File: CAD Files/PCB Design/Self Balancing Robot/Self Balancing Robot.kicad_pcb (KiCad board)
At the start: 2 copper layers, 14 parts, among them J1 Screw_Terminal_01x02, M1 Stepper_Motor_bipolar, M2 Stepper_Motor_bipolar, U1 DEVKIT_V1_ESP32-WROOM-32, U2 TSR_1-2450

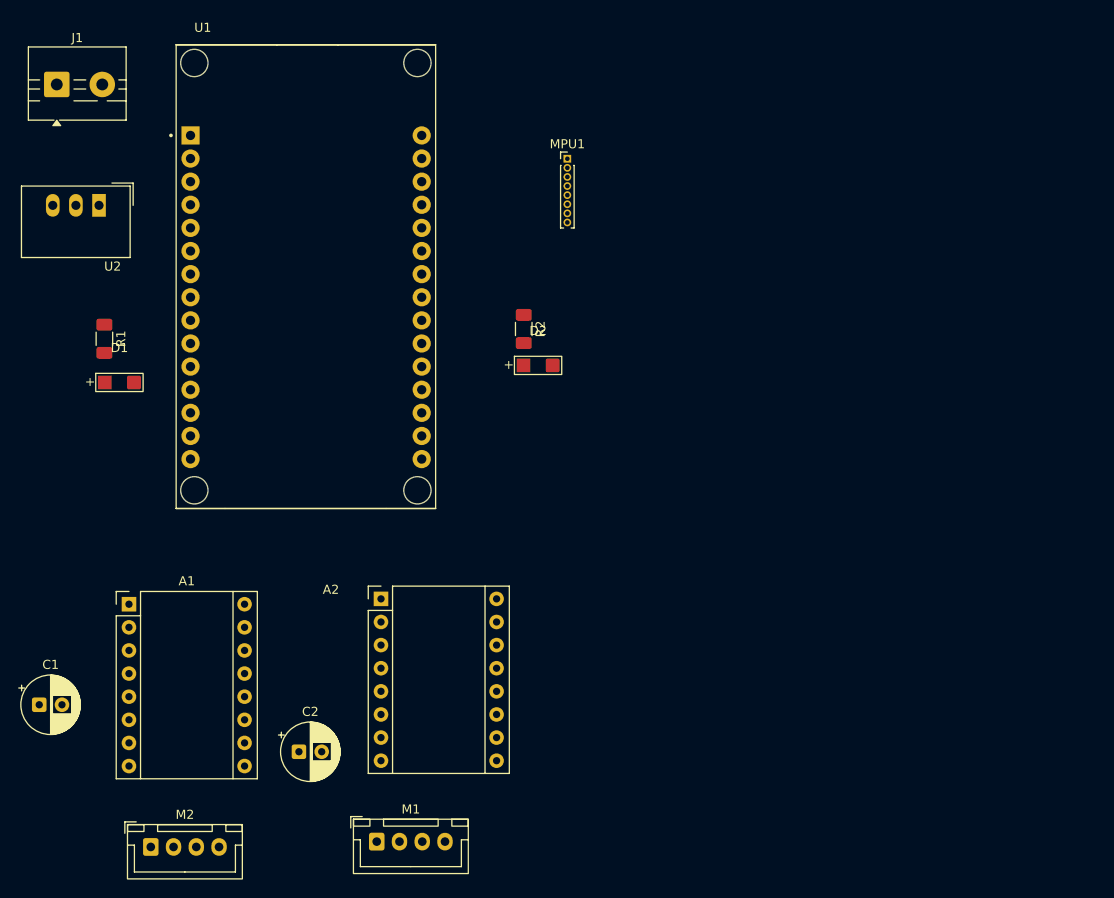
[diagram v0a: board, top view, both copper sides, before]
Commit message: Added MPU (GY-521) footprint
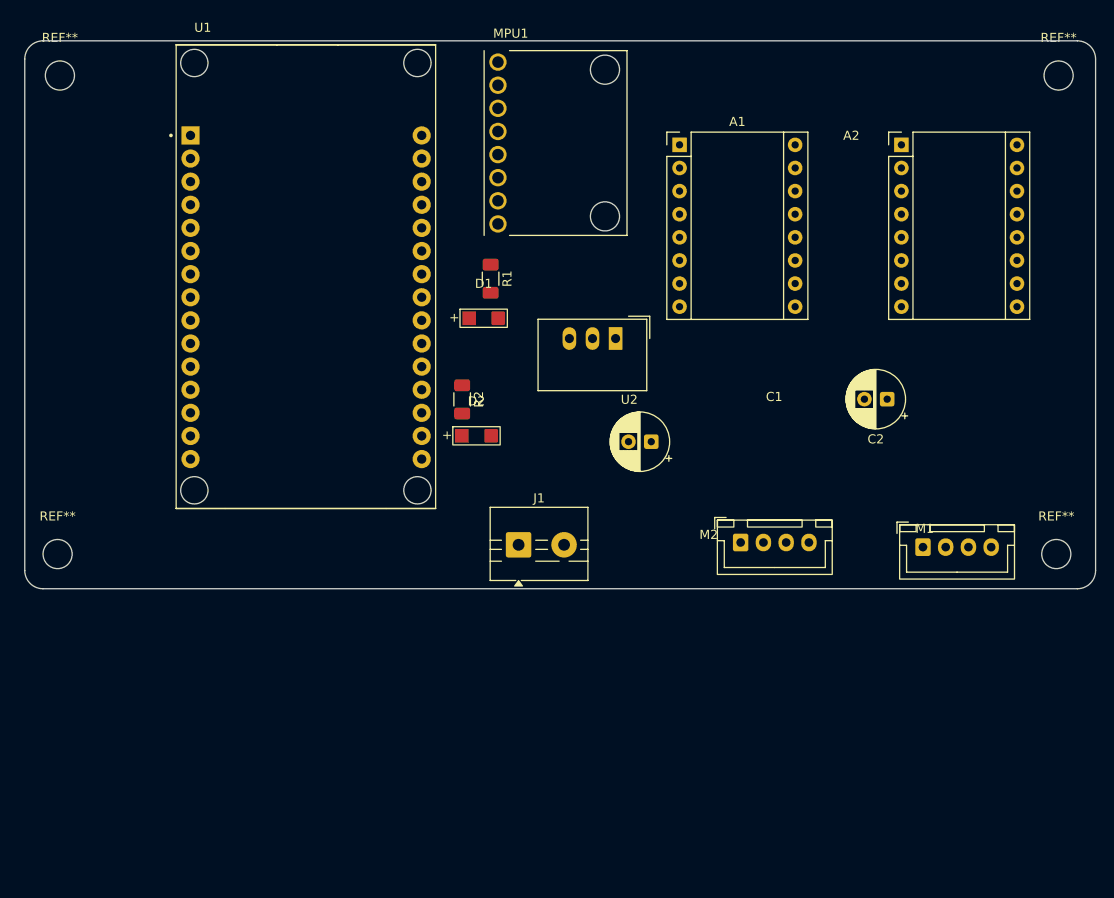
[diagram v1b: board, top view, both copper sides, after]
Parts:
- added REF**: MountingHole_3.2mm_M3, MountingHole:MountingHole_3.2mm_M3, F.Cu at (70.4, 89.2)
- added REF**: MountingHole_3.2mm_M3, MountingHole:MountingHole_3.2mm_M3, F.Cu at (180.1, 89.2)
- added REF**: MountingHole_3.2mm_M3, MountingHole:MountingHole_3.2mm_M3, F.Cu at (180.3, 36.6)
- added REF**: MountingHole_3.2mm_M3, MountingHole:MountingHole_3.2mm_M3, F.Cu at (70.6, 36.6)
- MPU1: footprint Connector_PinHeader_1.00mm:PinHeader_1x08_P1.00mm_Vertical -> TW Footprints:MODULE_GY-521
- moved A1 78.8 mm to (138.7, 44.2)
- moved A2 75.9 mm to (163.1, 44.2)
- moved C2 75.3 mm to (161.5, 72.1), turned to 180 degrees
- moved C1 73.2 mm to (135.6, 76.8), turned to 180 degrees
- moved M2 72.9 mm to (145.4, 87.9)
- moved J1 71.6 mm to (121.0, 88.1)
- moved M1 68.2 mm to (165.4, 88.4)
- moved U2 58.6 mm to (131.7, 65.5)
- moved R1 42.9 mm to (117.9, 58.9)
- moved D1 40.6 mm to (117.2, 63.2)
- moved D2 10.3 mm to (116.4, 76.2)
- moved R2 10.3 mm to (114.8, 72.2)
- moved MPU1 2.16 mm to (125.1, 44.0)
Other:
- board outline added: 117.7 x 60.2 mm
